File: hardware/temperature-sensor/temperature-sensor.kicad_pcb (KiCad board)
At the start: 2 copper layers, 56 x 56 mm, 32 parts, among them IC1 SHT40-CD1B-R3, IC2 PM8803TR, J1 1149611, T1 PT61018PEL, U1 STM32F407V_E-G_Tx, U2 LAN8720A, Y1 CX2016FB25000C0FZZH1

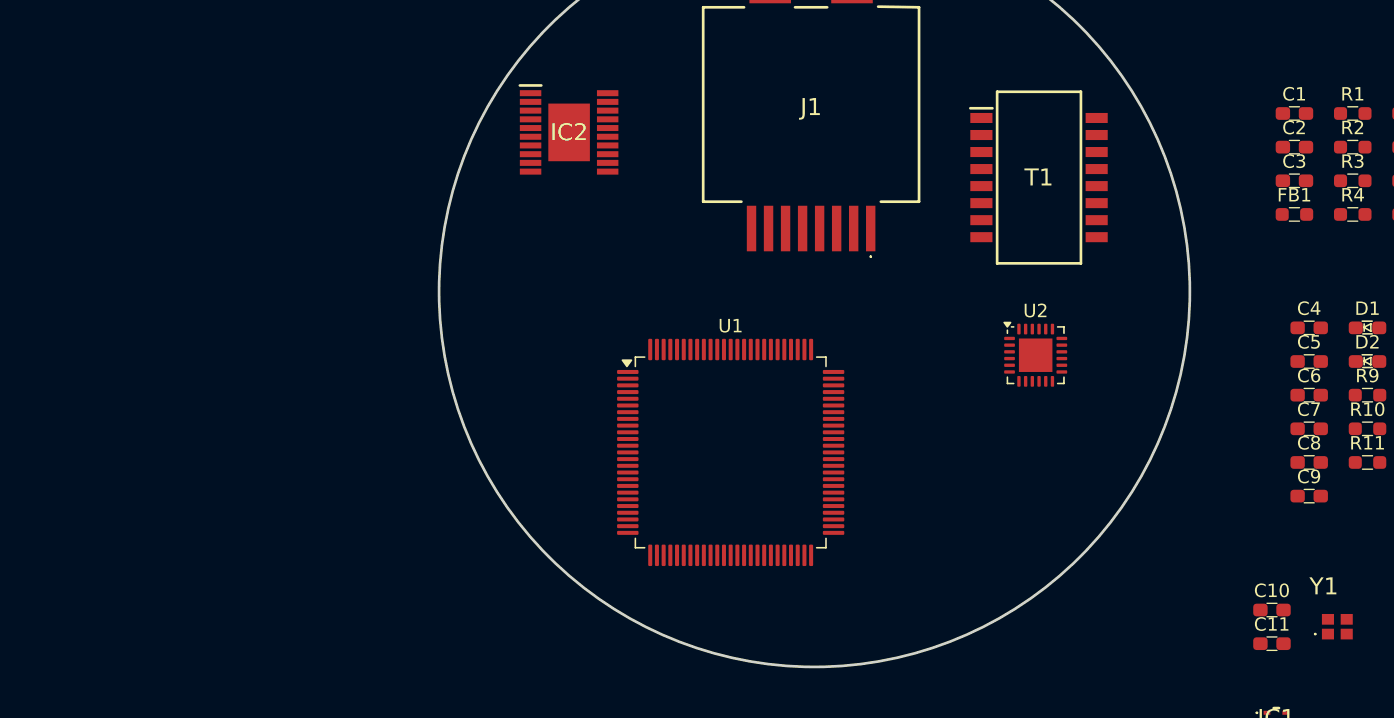
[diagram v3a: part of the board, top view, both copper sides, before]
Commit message: update PCB from schematic
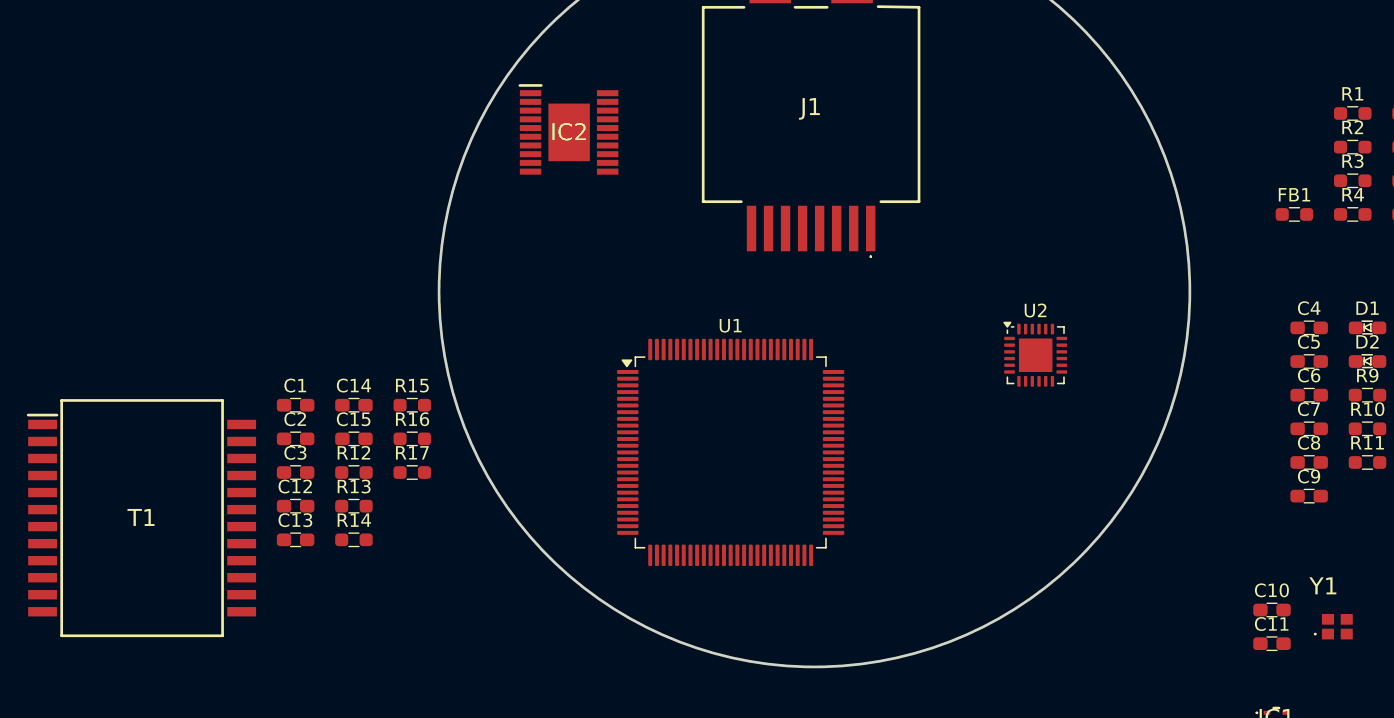
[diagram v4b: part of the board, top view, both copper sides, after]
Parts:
- added C12: 10nF 100V, benediktibk:C_0603_1608Metric_Pad1.08x0.95mm_HandSolder, F.Cu at (111.3, 115.0)
- added C13: 10nF 100V, benediktibk:C_0603_1608Metric_Pad1.08x0.95mm_HandSolder, F.Cu at (111.3, 117.5)
- added C14: 10nF 100V, benediktibk:C_0603_1608Metric_Pad1.08x0.95mm_HandSolder, F.Cu at (115.7, 107.5)
- added C15: 1nF 3kV, benediktibk:C_0603_1608Metric_Pad1.08x0.95mm_HandSolder, F.Cu at (115.7, 110.0)
- added R12: 75Ohm, benediktibk:R_0603_1608Metric_Pad0.98x0.95mm_HandSolder, F.Cu at (115.7, 112.5)
- added R13: 75Ohm, benediktibk:R_0603_1608Metric_Pad0.98x0.95mm_HandSolder, F.Cu at (115.7, 115.0)
- added R14: 75Ohm, benediktibk:R_0603_1608Metric_Pad0.98x0.95mm_HandSolder, F.Cu at (115.7, 117.5)
- added R15: 75Ohm, benediktibk:R_0603_1608Metric_Pad0.98x0.95mm_HandSolder, F.Cu at (120.0, 107.5)
- added R16: 75Ohm, benediktibk:R_0603_1608Metric_Pad0.98x0.95mm_HandSolder, F.Cu at (120.0, 110.0)
- added R17: 75Ohm, benediktibk:R_0603_1608Metric_Pad0.98x0.95mm_HandSolder, F.Cu at (120.0, 112.5)
- C1: value 1nF 1kV -> 1nF 3kV
- C2: value 100nF -> 1nF 3kV
- C3: value 100nF -> 10nF 100V
- T1: value PT61018PEL -> SM51625EL; footprint benediktibk:SOIC127P930X565-16N -> benediktibk:SOIC127P1600X625-24N
- moved C1 77.6 mm to (111.3, 107.5)
- moved C2 77.6 mm to (111.3, 110.0)
- moved C3 77.6 mm to (111.3, 112.5)
- moved T1 71.6 mm to (99.8, 115.9)
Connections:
- C2 pad 1: Net-(T1-CT_2) -> Net-(C2-Pad1)
- C3 pad 1: Net-(T1-CT_1) -> Net-(C3-Pad1)
- C3 pad 2: GND -> Net-(C12-Pad2)
- J1 pad 1: Net-(T1-TX+) -> Net-(T1-MX1+)
- J1 pad 2: Net-(T1-TX-) -> Net-(T1-MX1-)
- J1 pad 3: Net-(T1-RX+) -> Net-(T1-MX2+)
- J1 pad 4: Net-(J1-Pad4) -> Net-(T1-MX3+)
- J1 pad 5: Net-(J1-Pad4) -> Net-(T1-MX3-)
- J1 pad 6: Net-(T1-RX-) -> Net-(T1-MX2-)
- J1 pad 7: Net-(J1-Pad7) -> Net-(T1-MX4+)
- J1 pad 8: Net-(J1-Pad7) -> Net-(T1-MX4-)
- R2 pad 1: Net-(T1-CT_3) -> Net-(T1-MCT3)
- R3 pad 1: Net-(J1-Pad4) -> Net-(T1-MCT2)
- R4 pad 1: Net-(J1-Pad7) -> Net-(T1-MCT1)
- T1 pad 1: /Ethernet/TX_P -> Net-(T1-TCT1)
- T1 pad 10: Net-(T1-CT_3) -> Net-(T1-TCT4)
- T1 pad 11: Net-(T1-RX+) -> Net-(T1-TD4+)
- T1 pad 12: unconnected-(T1-NC_3-Pad12) -> Net-(T1-TD4+)
- T1 pad 13: unconnected-(T1-NC_4-Pad13) -> Net-(T1-MX4-)
- T1 pad 14: Net-(T1-TX-) -> Net-(T1-MX4+)
- T1 pad 16: Net-(T1-TX+) -> Net-(T1-MX3-)
- T1 pad 2: Net-(T1-CT_1) -> /Ethernet/TX_P
- T1 pad 4: unconnected-(T1-NC_1-Pad4) -> Net-(T1-TCT2)
- T1 pad 5: unconnected-(T1-NC_2-Pad5) -> /Ethernet/RX_P
- T1 pad 6: /Ethernet/RX_P -> /Ethernet/RX_N
- T1 pad 7: Net-(T1-CT_2) -> Net-(T1-TCT3)
- T1 pad 8: /Ethernet/RX_N -> Net-(T1-TD3+)
- T1 pad 9: Net-(T1-RX-) -> Net-(T1-TD3+)

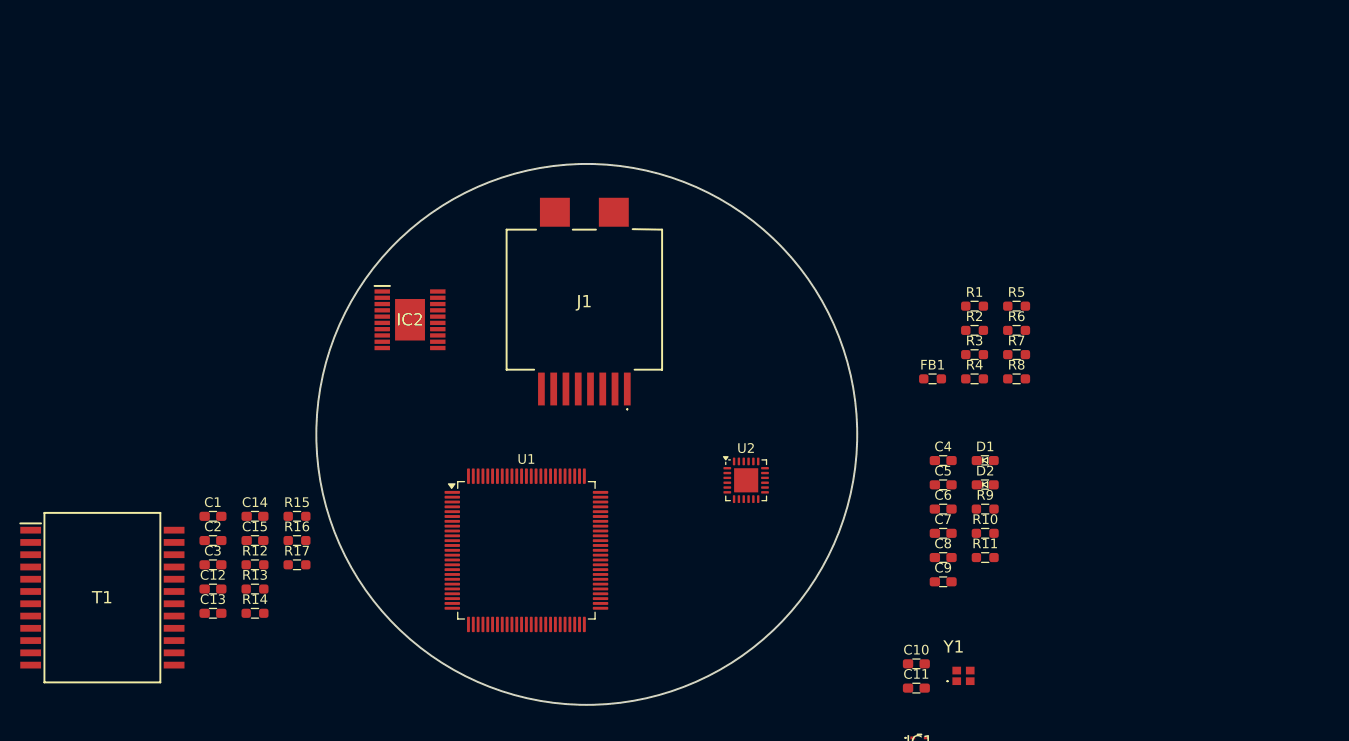
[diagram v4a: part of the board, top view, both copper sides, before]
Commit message: work on temperature sensor
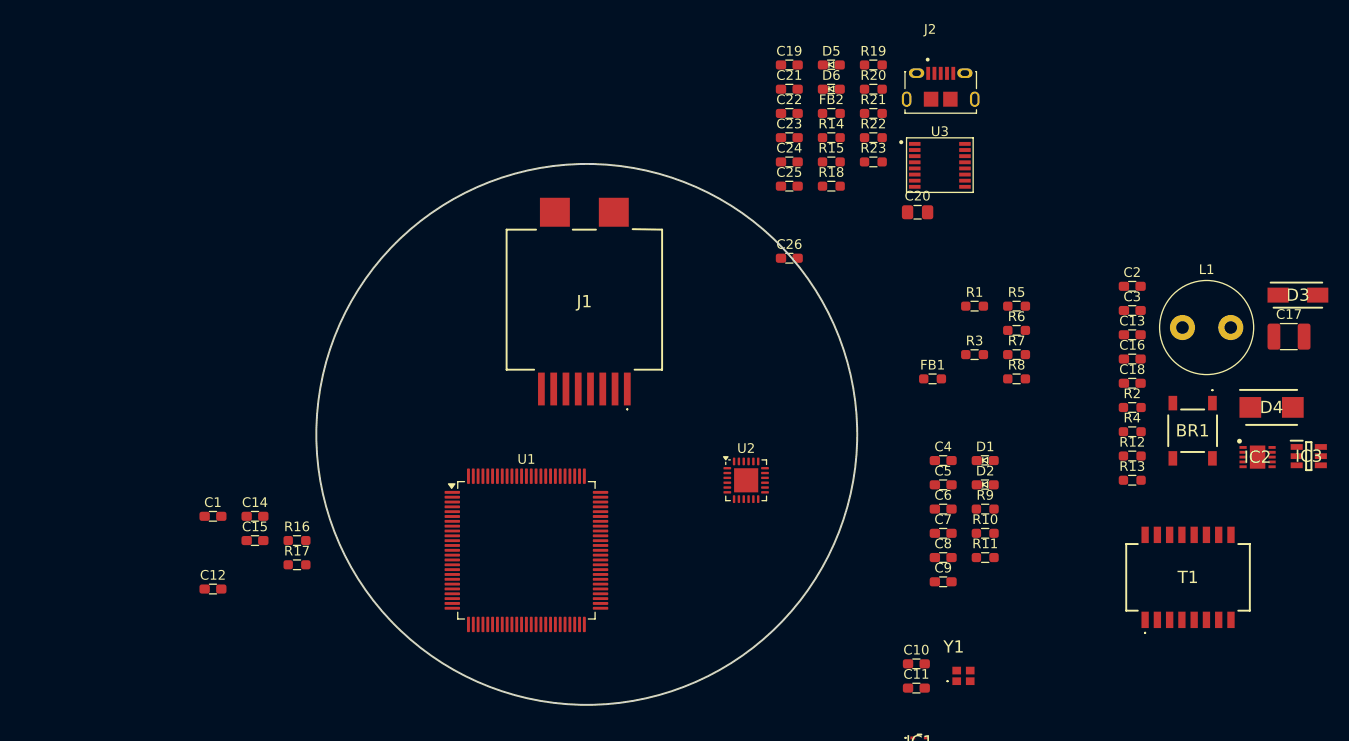
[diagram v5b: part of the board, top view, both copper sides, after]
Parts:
- added BR1: ABS8, benediktibk:ABS8, F.Cu at (212.7, 98.6)
- added C16: 68nF 100V, benediktibk:C_0603_1608Metric_Pad1.08x0.95mm_HandSolder, F.Cu at (206.5, 91.2)
- added C17: 10uF, benediktibk:C_1210_3225Metric_Pad1.33x2.70mm_HandSolder, F.Cu at (222.7, 88.9)
- added C18: 1uF, benediktibk:C_0603_1608Metric_Pad1.08x0.95mm_HandSolder, F.Cu at (206.5, 93.7)
- added C19: 10nF, benediktibk:C_0603_1608Metric_Pad1.08x0.95mm_HandSolder, F.Cu at (171.0, 60.8)
- added C20: 4.7uF, benediktibk:C_0805_2012Metric_Pad1.18x1.45mm_HandSolder, F.Cu at (184.2, 76.0)
- added C21: 100nF, benediktibk:C_0603_1608Metric_Pad1.08x0.95mm_HandSolder, F.Cu at (171.0, 63.3)
- added C22: 100nF, benediktibk:C_0603_1608Metric_Pad1.08x0.95mm_HandSolder, F.Cu at (171.0, 65.8)
- added C23: 47pF, benediktibk:C_0603_1608Metric_Pad1.08x0.95mm_HandSolder, F.Cu at (171.0, 68.3)
- added C24: 47pF, benediktibk:C_0603_1608Metric_Pad1.08x0.95mm_HandSolder, F.Cu at (171.0, 70.8)
- added C25: 100nF, benediktibk:C_0603_1608Metric_Pad1.08x0.95mm_HandSolder, F.Cu at (171.0, 73.3)
- added C26: C_100nF_SMD_0603_50V, benediktibk:C_0603_1608Metric_Pad1.08x0.95mm_HandSolder, F.Cu at (171.0, 80.8)
- added D3: SMAJ58A, benediktibk:DIOM5026X229N, F.Cu at (223.6, 84.6)
- added D4: B280-13-F, benediktibk:DIOM5336X250N, F.Cu at (220.9, 96.2)
- added D5: UART_TX, benediktibk:D_0603_1608Metric_Pad1.05x0.95mm_HandSolder, F.Cu at (175.3, 60.8)
- added D6: UART_RX, benediktibk:D_0603_1608Metric_Pad1.05x0.95mm_HandSolder, F.Cu at (175.3, 63.3)
- added FB2: BLM18P, benediktibk:R_0603_1608Metric_Pad0.98x0.95mm_HandSolder, F.Cu at (175.3, 65.8)
- added IC3: LV2862XLVDDCR, benediktibk:SOT95P280X110-6N, F.Cu at (224.8, 101.2)
- added J2: AMPHENOL_micro_usb_10118194-0001LF, benediktibk:AMPHENOL_10118194-0001LF, F.Cu at (186.6, 64.3)
- added L1: 22uH, benediktibk:L_Radial_D9.5mm_P5.00mm_Fastron_07HVP, F.Cu at (211.7, 87.9)
- added R18: 120Ohm, benediktibk:R_0603_1608Metric_Pad0.98x0.95mm_HandSolder, F.Cu at (175.3, 73.3)
- added R19: 120Ohm, benediktibk:R_0603_1608Metric_Pad0.98x0.95mm_HandSolder, F.Cu at (179.7, 60.8)
- added R20: 10kOhm, benediktibk:R_0603_1608Metric_Pad0.98x0.95mm_HandSolder, F.Cu at (179.7, 63.3)
- added R21: 10kOhm, benediktibk:R_0603_1608Metric_Pad0.98x0.95mm_HandSolder, F.Cu at (179.7, 65.8)
- added R22: 10kOhm, benediktibk:R_0603_1608Metric_Pad0.98x0.95mm_HandSolder, F.Cu at (179.7, 68.3)
- added R23: 10kOhm, benediktibk:R_0603_1608Metric_Pad0.98x0.95mm_HandSolder, F.Cu at (179.7, 70.8)
- added U3: FT230XS, benediktibk:SSOP-16_3.9x4.9mm_P0.635mm, F.Cu at (186.6, 71.1)
- C13: value 10nF 100V -> 100nF
- C2: value 1nF 3kV -> 1uF 100V
- C3: value 10nF 100V -> 1uF 100V
- IC2: value PM8803TR -> MAX5969BETB+T; footprint benediktibk:SOP65P640X120-21N -> benediktibk:SON50P300X300X80-11N
- R12: value 75Ohm -> 10kOhm
- R13: value 75Ohm -> 33kOhm
- R14, R15: value 75Ohm -> 27Ohm
- R2: value 75Ohm -> 619Ohm
- R4: value 75Ohm -> 24.9kOhm
- T1: value SM51625EL -> SM13126PEL; footprint benediktibk:SOIC127P1600X625-24N -> benediktibk:SM13126PEL
- moved T1 112.4 mm to (212.2, 113.8)
- moved C13 99.4 mm to (206.5, 88.7)
- moved C3 98.7 mm to (206.5, 86.2)
- moved C2 98.7 mm to (206.5, 83.7)
- moved R12 91.5 mm to (206.5, 101.2)
- moved R13 91.5 mm to (206.5, 103.7)
- moved IC2 88.9 mm to (219.4, 101.3)
- moved R14 77.4 mm to (175.3, 68.3)
- moved R15 66.4 mm to (175.3, 70.8)
- moved R2 18.2 mm to (206.5, 96.2)
- moved R4 17.2 mm to (206.5, 98.7)
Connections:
- net Net-(T1-TCT3) renamed /Ethernet/CT2
- C13 pad 1: Net-(C13-Pad1) -> Net-(D4-K)
- C13 pad 2: Net-(C12-Pad2) -> Net-(IC3-CB)
- C2 pad 1: Net-(C2-Pad1) -> Net-(BR1-+)
- C3 pad 1: Net-(C3-Pad1) -> Net-(BR1-+)
- C3 pad 2: Net-(C12-Pad2) -> GND
- IC1 pad 1: unconnected-(IC1-SDA-Pad1) -> /Measurement/SDA
- IC1 pad 2: unconnected-(IC1-SCL-Pad2) -> /Measurement/SCL
- IC1 pad 3: unconnected-(IC1-VDD-Pad3) -> /Measurement/3V3
- IC1 pad 4: unconnected-(IC1-VSS-Pad4) -> GND
- IC2 pad 1: unconnected-(IC2-CTL-Pad1) -> Net-(BR1-+)
- IC2 pad 10: unconnected-(IC2-VSS-Pad10) -> Net-(IC2-CLS)
- IC2 pad 11: unconnected-(IC2-VDD_1-Pad11) -> GND
- IC2 pad 2: unconnected-(IC2-VB-Pad2) -> Net-(IC2-DET)
- IC2 pad 6: unconnected-(IC2-VC-Pad6) -> Net-(IC2-RTN)
- IC2 pad 7: unconnected-(IC2-GAT2-Pad7) -> Net-(IC2-RTN)
- IC2 pad 8: unconnected-(IC2-ARTN-Pad8) -> Net-(IC2-PG)
- J1 pad 1: Net-(T1-MX1+) -> Net-(T1-TX1+)
- J1 pad 2: Net-(T1-MX1-) -> Net-(T1-TX1-)
- J1 pad 3: Net-(T1-MX2+) -> Net-(T1-TX2+)
- J1 pad 4: Net-(T1-MX3+) -> unconnected-(J1-Pad4)
- J1 pad 5: Net-(T1-MX3-) -> unconnected-(J1-Pad5)
- J1 pad 6: Net-(T1-MX2-) -> Net-(T1-TX2-)
- J1 pad 7: Net-(T1-MX4+) -> unconnected-(J1-Pad7)
- J1 pad 8: Net-(T1-MX4-) -> unconnected-(J1-Pad8)
- R1 pad 1: Net-(T1-MCT4) -> Net-(T1-CT2_2)
- R12 pad 1: Net-(T1-TD4+) -> Net-(IC3-FB)
- R12 pad 2: Net-(C2-Pad1) -> GND
- R13 pad 1: Net-(T1-TD3+) -> /Power over Ethernet/3V3
- R13 pad 2: Net-(C2-Pad1) -> Net-(IC3-FB)
- R14 pad 1: Net-(T1-TCT2) -> Net-(U3-USBDM)
- R14 pad 2: Net-(C13-Pad1) -> Net-(J2-D-)
- R15 pad 1: Net-(T1-TCT4) -> Net-(U3-USBDP)
- R15 pad 2: Net-(C3-Pad1) -> Net-(J2-D+)
- R16 pad 1: Net-(T1-TCT1) -> /Ethernet/CT1
- R2 pad 1: Net-(T1-MCT3) -> Net-(IC2-CLS)
- R2 pad 2: Net-(C1-Pad1) -> GND
- R3 pad 1: Net-(T1-MCT2) -> Net-(T1-CT1_2)
- R4 pad 1: Net-(T1-MCT1) -> Net-(BR1-+)
- R4 pad 2: Net-(C1-Pad1) -> Net-(IC2-DET)
- T1 pad 1: Net-(T1-TCT1) -> /Ethernet/TX_P
- T1 pad 10: Net-(T1-TCT4) -> Net-(T1-CT2_2)
- T1 pad 11: Net-(T1-TD4+) -> Net-(T1-TX2+)
- T1 pad 12: Net-(T1-TD4+) -> unconnected-(T1-NC_3-Pad12)
- T1 pad 13: Net-(T1-MX4-) -> unconnected-(T1-NC_4-Pad13)
- T1 pad 14: Net-(T1-MX4+) -> Net-(T1-TX1-)
- T1 pad 15: Net-(T1-MCT4) -> Net-(T1-CT1_2)
- T1 pad 16: Net-(T1-MX3-) -> Net-(T1-TX1+)
- T1 pad 2: /Ethernet/TX_P -> /Ethernet/CT1
- T1 pad 4: Net-(T1-TCT2) -> unconnected-(T1-NC_1-Pad4)
- T1 pad 5: /Ethernet/RX_P -> unconnected-(T1-NC_2-Pad5)
- T1 pad 6: /Ethernet/RX_N -> /Ethernet/RX_P
- T1 pad 8: Net-(T1-TD3+) -> /Ethernet/RX_N
- T1 pad 9: Net-(T1-TD3+) -> Net-(T1-TX2-)
- U2 pad 14: /Ethernet/REFCLK -> unconnected-(U2-~{INT}/REFCLKO-Pad14)
